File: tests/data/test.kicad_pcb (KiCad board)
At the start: 2 copper layers, 1 part

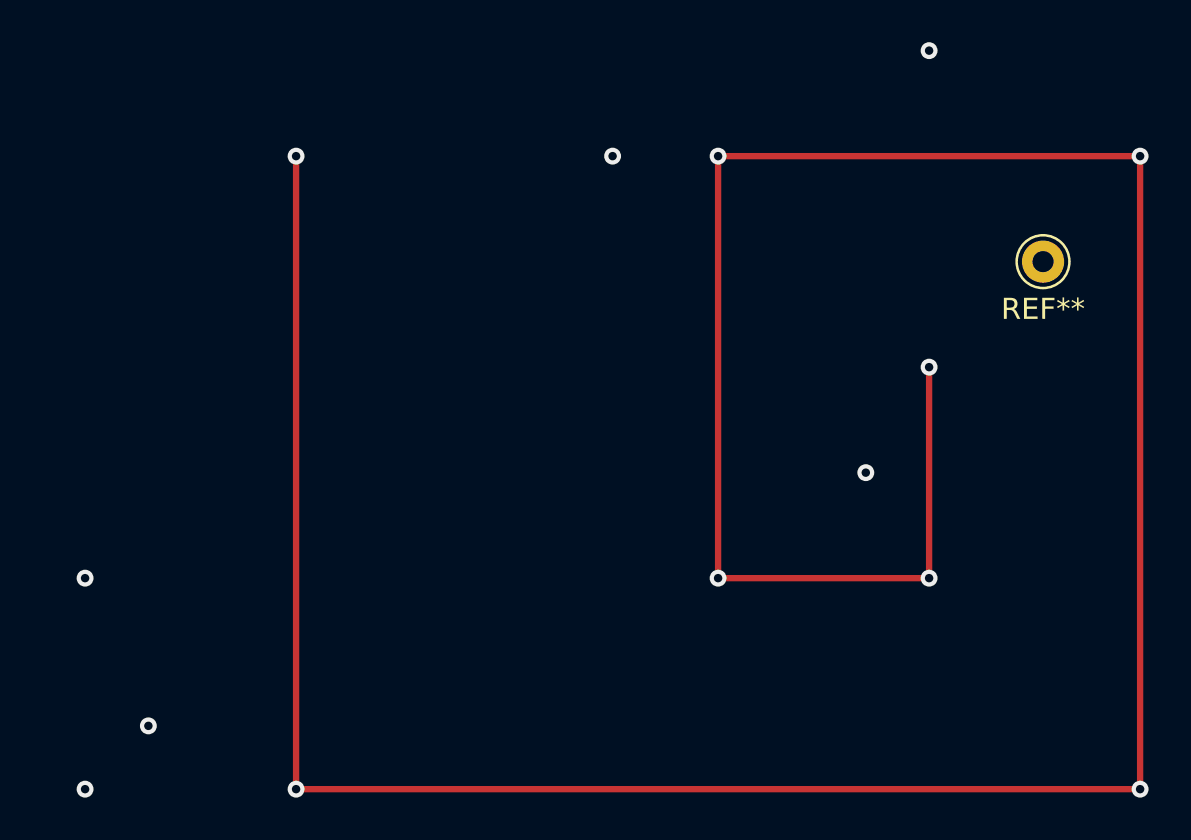
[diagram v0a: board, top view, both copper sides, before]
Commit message: dsn,tests: use pins instead of vias in test .dsn file
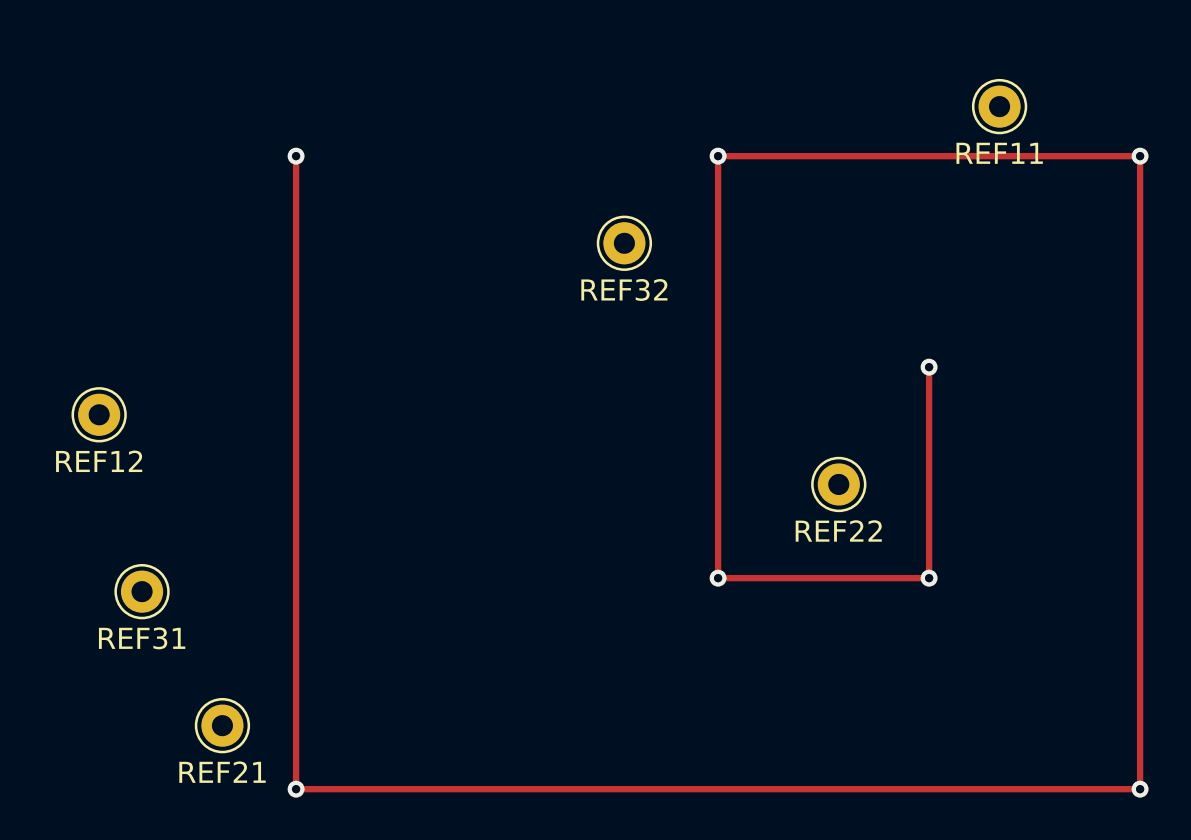
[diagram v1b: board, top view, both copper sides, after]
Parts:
- added REF12: Pin_D1.0mm_L10.0mm, Connector_Pin:Pin_D1.0mm_L10.0mm, F.Cu at (10.7, 32.3)
- added REF21: Pin_D1.0mm_L10.0mm, Connector_Pin:Pin_D1.0mm_L10.0mm, F.Cu at (16.5, 47.0)
- added REF22: Pin_D1.0mm_L10.0mm, Connector_Pin:Pin_D1.0mm_L10.0mm, F.Cu at (45.7, 35.6)
- added REF31: Pin_D1.0mm_L10.0mm, Connector_Pin:Pin_D1.0mm_L10.0mm, F.Cu at (12.7, 40.6)
- added REF32: Pin_D1.0mm_L10.0mm, Connector_Pin:Pin_D1.0mm_L10.0mm, F.Cu at (35.6, 24.1)
- moved REF11 7.63 mm to (53.3, 17.7)
- renumbered REF** to REF11
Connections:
- REF11 pad 1: (no net) -> 1
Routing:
- net 5: track 160.0 -> 0.00 mm, vias 8 -> 0
- net 3: track 0.00 -> 160.0 mm, vias 2 -> 8
- net 2: vias 2 -> 0
- net 1: vias 2 -> 0

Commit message: dsn, rules: fix import bugs, update test file
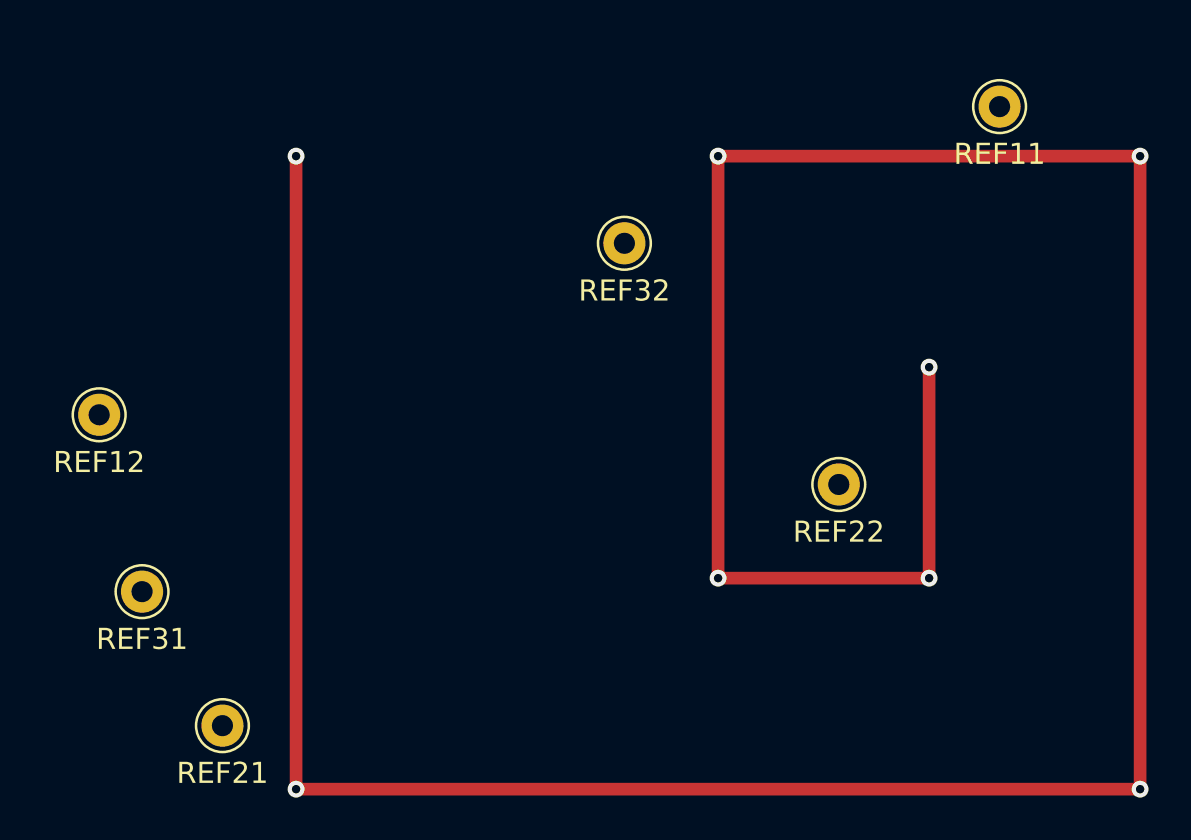
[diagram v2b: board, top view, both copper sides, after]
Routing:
- net unconnected: track 0.00 -> 160.0 mm, vias 0 -> 8
- net 3: track 160.0 -> 0.00 mm, vias 8 -> 0
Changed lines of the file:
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@@
   (net 2 "2")
   (net 3 "3")
+  (net 4 "unconnected")
   (footprint "Connector_Pin:Pin_D1.0mm_L10.0mm" (layer "F.Cu")
     (at 16.51 46.99)
@@
     )
   )
-  (segment (start 20 50) (end 60 50) (width 0.3) (layer "F.Cu") (net 3))
-  (segment (start 60 20) (end 40 20) (width 0.3) (layer "F.Cu") (net 3))
-  (segment (start 40 20) (end 40 40) (width 0.3) (layer "F.Cu") (net 3))
-  (segment (start 50 40) (end 50 30) (width 0.3) (layer "F.Cu") (net 3))
-  (segment (start 60 50) (end 60 20) (width 0.3) (layer "F.Cu") (net 3))
-  (segment (start 20 20) (end 20 50) (width 0.3) (layer "F.Cu") (net 3))
-  (segment (start 40 40) (end 50 40) (width 0.3) (layer "F.Cu") (net 3))
-  (via (at 20 50) (size 0.8) (drill 0.4) (layers "F.Cu" "B.Cu") (net 3))
-  (via (at 20 20) (size 0.8) (drill 0.4) (layers "F.Cu" "B.Cu") (net 3))
-  (via (at 40 20) (size 0.8) (drill 0.4) (layers "F.Cu" "B.Cu") (net 3))
-  (via (at 60 50) (size 0.8) (drill 0.4) (layers "F.Cu" "B.Cu") (net 3))
-  (via (at 50 30) (size 0.8) (drill 0.4) (layers "F.Cu" "B.Cu") (net 3))
-  (via (at 40 40) (size 0.8) (drill 0.4) (layers "F.Cu" "B.Cu") (net 3))
-  (via (at 60 20) (size 0.8) (drill 0.4) (layers "F.Cu" "B.Cu") (net 3))
-  (via (at 50 40) (size 0.8) (drill 0.4) (layers "F.Cu" "B.Cu") (net 3))
+  (segment (start 20 50) (end 60 50) (width 0.6) (layer "F.Cu") (net 4))
+  (segment (start 60 20) (end 40 20) (width 0.6) (layer "F.Cu") (net 4))
+  (segment (start 40 20) (end 40 40) (width 0.6) (layer "F.Cu") (net 4))
+  (segment (start 50 40) (end 50 30) (width 0.6) (layer "F.Cu") (net 4))
+  (segment (start 60 50) (end 60 20) (width 0.6) (layer "F.Cu") (net 4))
+  (segment (start 20 20) (end 20 50) (width 0.6) (layer "F.Cu") (net 4))
+  (segment (start 40 40) (end 50 40) (width 0.6) (layer "F.Cu") (net 4))
+  (via (at 20 50) (size 0.8) (drill 0.4) (layers "F.Cu" "B.Cu") (free) (net 4))
+  (via (at 60 50) (size 0.8) (drill 0.4) (layers "F.Cu" "B.Cu") (free) (net 4))
+  (via (at 50 40) (size 0.8) (drill 0.4) (layers "F.Cu" "B.Cu") (free) (net 4))
+  (via (at 40 20) (size 0.8) (drill 0.4) (layers "F.Cu" "B.Cu") (free) (net 4))
+  (via (at 20 20) (size 0.8) (drill 0.4) (layers "F.Cu" "B.Cu") (free) (net 4))
+  (via (at 40 40) (size 0.8) (drill 0.4) (layers "F.Cu" "B.Cu") (free) (net 4))
+  (via (at 60 20) (size 0.8) (drill 0.4) (layers "F.Cu" "B.Cu") (free) (net 4))
+  (via (at 50 30) (size 0.8) (drill 0.4) (layers "F.Cu" "B.Cu") (free) (net 4))
 )
